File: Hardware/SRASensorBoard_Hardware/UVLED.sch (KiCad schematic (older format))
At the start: 8 parts

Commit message: Sciency stuff for the board
finished!
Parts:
- added D?: LED, Diode_SMD:D_0603_1608Metric_Pad1.05x0.95mm_HandSolder, symbol Device:LED
- added R?: 330, Resistor_SMD:R_0603_1608Metric_Pad1.05x0.95mm_HandSolder, symbol Device:R
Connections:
- net GND: now also D?.1 (K)
- net LED_Enable: now also R?.1
- new net: D?.2 (A), R?.2
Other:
- note added: "YELLOW"
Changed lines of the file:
@@
 Wire Wire Line
 	6350 3350 6500 3350
-Text GLabel 5250 3850 0    50   Input ~ 0
+Text GLabel 5125 4025 2    50   Input ~ 0
 LED_Enable
 $Comp
@@
 $EndComp
 Wire Wire Line
-	5250 3850 5350 3850
-Wire Wire Line
 	5750 3500 5750 3850
 Wire Wire Line
@@
 Wire Wire Line
 	4900 3050 6100 3050
+$Comp
+L Device:LED D?
+U 1 1 604F1096
+P 4550 3850
+AR Path="/604F1096" Ref="D?"  Part="1"
+AR Path="/5F841BF9/604F1096" Ref="D?"  Part="1"
+F 0 "D?" V 4589 3733 50  0000 R CNN
+F 1 "LED" V 4498 3733 50  0000 R CNN
+F 2 "Diode_SMD:D_0603_1608Metric_Pad1.05x0.95mm_HandSolder" H 4550 3850 50  0001 C CNN
+F 3 "~" H 4550 3850 50  0001 C CNN
+	1    4550 3850
+	1    0    0    -1
+$EndComp
+$Comp
+L Device:R R?
+U 1 1 604F109C
+P 4950 3850
+AR Path="/604F109C" Ref="R?"  Part="1"
+AR Path="/5F841BF9/604F109C" Ref="R?"  Part="1"
+F 0 "R?" H 5020 3896 50  0000 L CNN
+F 1 "330" H 5020 3805 50  0000 L CNN
+F 2 "Resistor_SMD:R_0603_1608Metric_Pad1.05x0.95mm_HandSolder" V 4880 3850 50  0001 C CNN
+F 3 "~" H 4950 3850 50  0001 C CNN
+	1    4950 3850
+	0    1    1    0
+$EndComp
+Text Notes 3875 3950 0    50   ~ 0
+YELLOW
+Wire Wire Line
+	4700 3850 4800 3850
+$Comp
+L power:GND #PWR?
+U 1 1 604F1131
+P 4250 3950
+AR Path="/604F1131" Ref="#PWR?"  Part="1"
+AR Path="/5F841BF9/604F1131" Ref="#PWR?"  Part="1"
+F 0 "#PWR?" H 4250 3700 50  0001 C CNN
+F 1 "GND" H 4350 3850 50  0000 C CNN
+F 2 "" H 4250 3950 50  0001 C CNN
+F 3 "" H 4250 3950 50  0001 C CNN
+	1    4250 3950
+	1    0    0    -1
+$EndComp
+Wire Wire Line
+	5100 3850 5125 3850
+Wire Wire Line
+	4250 3850 4250 3950
+Wire Wire Line
+	4250 3850 4400 3850
+Wire Wire Line
+	5125 4025 5125 3850
+Connection ~ 5125 3850
+Wire Wire Line
+	5125 3850 5350 3850
 $EndSCHEMATC

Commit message: Science_sensor reveiw 1
Yep
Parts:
- Q8: renamed from Q?; footprint Package_TO_SOT_SMD:SOT-23 -> Package_TO_SOT_SMD:TO-252-2
- gave numbers to parts that had none: 8
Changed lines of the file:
@@
 P 6250 3050
 AR Path="/5F8D9123" Ref="R?"  Part="1"
-AR Path="/5F8CBD9C/5F8D9123" Ref="R?"  Part="1"
+AR Path="/5F8CBD9C/5F8D9123" Ref="R37"  Part="1"
 AR Path="/5F8FEC08/5F8D9123" Ref="R?"  Part="1"
-F 0 "R?" V 6150 3050 50  0000 C CNN
+F 0 "R37" V 6150 3050 50  0000 C CNN
 F 1 "4" V 6250 3050 50  0000 C CNN
 F 2 "Resistor_THT:R_Axial_DIN0414_L11.9mm_D4.5mm_P15.24mm_Horizontal" V 6180 3050 50  0001 C CNN
@@
 P 6350 3350
 AR Path="/5F8D912A" Ref="#PWR?"  Part="1"
-AR Path="/5F8CBD9C/5F8D912A" Ref="#PWR?"  Part="1"
+AR Path="/5F8CBD9C/5F8D912A" Ref="#PWR0162"  Part="1"
 AR Path="/5F8FEC08/5F8D912A" Ref="#PWR?"  Part="1"
-F 0 "#PWR?" H 6350 3100 50  0001 C CNN
+F 0 "#PWR0162" H 6350 3100 50  0001 C CNN
 F 1 "GND" H 6355 3177 50  0000 C CNN
 F 2 "" H 6350 3350 50  0001 C CNN
@@
 P 6900 2950
 AR Path="/5F8D9132" Ref="Conn?"  Part="2"
-AR Path="/5F8CBD9C/5F8D9132" Ref="Conn?"  Part="2"
+AR Path="/5F8CBD9C/5F8D9132" Ref="Conn9"  Part="2"
 AR Path="/5F8FEC08/5F8D9132" Ref="Conn?"  Part="2"
-F 0 "Conn?" H 6872 2997 60  0000 R CNN
+F 0 "Conn9" H 6872 2997 60  0000 R CNN
 F 1 "UV_led" H 6872 3103 60  0000 R CNN
 F 2 "MRDT_Connectors:Anderson_2_Horizontal_Side_by_Side" H 6750 2400 60  0001 C CNN
@@
 P 6900 3250
 AR Path="/5F8D9138" Ref="Conn?"  Part="1"
-AR Path="/5F8CBD9C/5F8D9138" Ref="Conn?"  Part="1"
+AR Path="/5F8CBD9C/5F8D9138" Ref="Conn9"  Part="1"
 AR Path="/5F8FEC08/5F8D9138" Ref="Conn?"  Part="1"
-F 0 "Conn?" H 6872 3297 60  0000 R CNN
+F 0 "Conn9" H 6872 3297 60  0000 R CNN
 F 1 "UV_led" H 6872 3403 60  0000 R CNN
 F 2 "MRDT_Connectors:Anderson_2_Horizontal_Side_by_Side" H 6750 2700 60  0001 C CNN
@@
 P 4700 3150
 AR Path="/5F8D913E" Ref="Q?"  Part="1"
-AR Path="/5F8CBD9C/5F8D913E" Ref="Q?"  Part="1"
+AR Path="/5F8CBD9C/5F8D913E" Ref="Q7"  Part="1"
 AR Path="/5F8FEC08/5F8D913E" Ref="Q?"  Part="1"
-F 0 "Q?" V 5043 3150 50  0000 C CNN
+F 0 "Q7" V 5043 3150 50  0000 C CNN
 F 1 "Q_PMOS_GDS" V 4952 3150 50  0000 C CNN
 F 2 "Package_TO_SOT_SMD:TO-252-2" H 4900 3250 50  0001 C CNN
@@
 P 5350 3600
 AR Path="/5F8D9144" Ref="Q?"  Part="1"
-AR Path="/5F8CBD9C/5F8D9144" Ref="Q?"  Part="1"
+AR Path="/5F8CBD9C/5F8D9144" Ref="Q8"  Part="1"
 AR Path="/5F8FEC08/5F8D9144" Ref="Q?"  Part="1"
-F 0 "Q?" V 5700 3550 50  0000 L CNN
+F 0 "Q8" V 5700 3550 50  0000 L CNN
 F 1 "Q_NMOS_GSD" V 5600 3350 50  0000 L CNN
-F 2 "Package_TO_SOT_SMD:SOT-23" H 5550 3700 50  0001 C CNN
+F 2 "Package_TO_SOT_SMD:TO-252-2" H 5550 3700 50  0001 C CNN
 F 3 "~" H 5350 3600 50  0001 C CNN
 	1    5350 3600
@@
 P 4500 3500
 AR Path="/5F8D914A" Ref="R?"  Part="1"
-AR Path="/5F8CBD9C/5F8D914A" Ref="R?"  Part="1"
+AR Path="/5F8CBD9C/5F8D914A" Ref="R33"  Part="1"
 AR Path="/5F8FEC08/5F8D914A" Ref="R?"  Part="1"
-F 0 "R?" V 4600 3450 50  0000 L CNN
+F 0 "R33" V 4600 3450 50  0000 L CNN
 F 1 "22k" V 4500 3500 50  0000 C CNN
 F 2 "Resistor_SMD:R_0603_1608Metric_Pad1.05x0.95mm_HandSolder" V 4430 3500 50  0001 C CNN
@@
 P 4900 3500
 AR Path="/5F8D9150" Ref="R?"  Part="1"
-AR Path="/5F8CBD9C/5F8D9150" Ref="R?"  Part="1"
+AR Path="/5F8CBD9C/5F8D9150" Ref="R34"  Part="1"
 AR Path="/5F8FEC08/5F8D9150" Ref="R?"  Part="1"
-F 0 "R?" V 5000 3450 50  0000 L CNN
+F 0 "R34" V 5000 3450 50  0000 L CNN
 F 1 "22k" V 4900 3500 50  0000 C CNN
 F 2 "Resistor_SMD:R_0603_1608Metric_Pad1.05x0.95mm_HandSolder" V 4830 3500 50  0001 C CNN
@@
 P 5750 3950
 AR Path="/5F8D915B" Ref="#PWR?"  Part="1"
-AR Path="/5F8CBD9C/5F8D915B" Ref="#PWR?"  Part="1"
+AR Path="/5F8CBD9C/5F8D915B" Ref="#PWR0163"  Part="1"
 AR Path="/5F8FEC08/5F8D915B" Ref="#PWR?"  Part="1"
-F 0 "#PWR?" H 5750 3700 50  0001 C CNN
+F 0 "#PWR0163" H 5750 3700 50  0001 C CNN
 F 1 "GND" H 5755 3777 50  0000 C CNN
 F 2 "" H 5750 3950 50  0001 C CNN
@@
 P 5550 3850
 AR Path="/5F8D9162" Ref="R?"  Part="1"
-AR Path="/5F8CBD9C/5F8D9162" Ref="R?"  Part="1"
+AR Path="/5F8CBD9C/5F8D9162" Ref="R36"  Part="1"
 AR Path="/5F8FEC08/5F8D9162" Ref="R?"  Part="1"
-F 0 "R?" V 5450 3800 50  0000 L CNN
+F 0 "R36" V 5450 3800 50  0000 L CNN
 F 1 "10k" V 5550 3850 50  0000 C CNN
 F 2 "Resistor_SMD:R_0603_1608Metric_Pad1.05x0.95mm_HandSolder" V 5480 3850 50  0001 C CNN
@@
 P 4200 3000
 AR Path="/5F8D9170" Ref="#PWR?"  Part="1"
-AR Path="/5F8CBD9C/5F8D9170" Ref="#PWR?"  Part="1"
+AR Path="/5F8CBD9C/5F8D9170" Ref="#PWR0164"  Part="1"
 AR Path="/5F8FEC08/5F8D9170" Ref="#PWR?"  Part="1"
-F 0 "#PWR?" H 4200 2850 50  0001 C CNN
+F 0 "#PWR0164" H 4200 2850 50  0001 C CNN
 F 1 "+24V" H 4215 3173 50  0000 C CNN
 F 2 "" H 4200 3000 50  0001 C CNN
@@
 AR Path="/604F1096" Ref="D?"  Part="1"
 AR Path="/5F841BF9/604F1096" Ref="D?"  Part="1"
-F 0 "D?" V 4589 3733 50  0000 R CNN
+AR Path="/5F8CBD9C/604F1096" Ref="D19"  Part="1"
+F 0 "D19" V 4589 3733 50  0000 R CNN
 F 1 "LED" V 4498 3733 50  0000 R CNN
 F 2 "Diode_SMD:D_0603_1608Metric_Pad1.05x0.95mm_HandSolder" H 4550 3850 50  0001 C CNN
@@
 AR Path="/604F109C" Ref="R?"  Part="1"
 AR Path="/5F841BF9/604F109C" Ref="R?"  Part="1"
-F 0 "R?" H 5020 3896 50  0000 L CNN
+AR Path="/5F8CBD9C/604F109C" Ref="R35"  Part="1"
+F 0 "R35" H 5020 3896 50  0000 L CNN
 F 1 "330" H 5020 3805 50  0000 L CNN
 F 2 "Resistor_SMD:R_0603_1608Metric_Pad1.05x0.95mm_HandSolder" V 4880 3850 50  0001 C CNN
@@
 AR Path="/604F1131" Ref="#PWR?"  Part="1"
 AR Path="/5F841BF9/604F1131" Ref="#PWR?"  Part="1"
-F 0 "#PWR?" H 4250 3700 50  0001 C CNN
+AR Path="/5F8CBD9C/604F1131" Ref="#PWR0165"  Part="1"
+F 0 "#PWR0165" H 4250 3700 50  0001 C CNN
 F 1 "GND" H 4350 3850 50  0000 C CNN
 F 2 "" H 4250 3950 50  0001 C CNN

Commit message: Fixed some library issues
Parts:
- R33, R34, R36: footprint Resistor_SMD:R_0603_1608Metric_Pad1.05x0.95mm_HandSolder -> Resistor_SMD:R_0603_1608Metric_Pad0.98x0.95mm_HandSolder
- R35: value 330 -> 480; footprint Resistor_SMD:R_0603_1608Metric_Pad1.05x0.95mm_HandSolder -> Resistor_SMD:R_0603_1608Metric_Pad0.98x0.95mm_HandSolder
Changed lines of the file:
@@
 EESchema Schematic File Version 4
+LIBS:SRA_Sensor_Board-cache
 EELAYER 30 0
 EELAYER END
@@
 F 0 "R33" V 4600 3450 50  0000 L CNN
 F 1 "22k" V 4500 3500 50  0000 C CNN
-F 2 "Resistor_SMD:R_0603_1608Metric_Pad1.05x0.95mm_HandSolder" V 4430 3500 50  0001 C CNN
+F 2 "Resistor_SMD:R_0603_1608Metric_Pad0.98x0.95mm_HandSolder" V 4430 3500 50  0001 C CNN
 F 3 "~" H 4500 3500 50  0001 C CNN
 	1    4500 3500
@@
 F 0 "R34" V 5000 3450 50  0000 L CNN
 F 1 "22k" V 4900 3500 50  0000 C CNN
-F 2 "Resistor_SMD:R_0603_1608Metric_Pad1.05x0.95mm_HandSolder" V 4830 3500 50  0001 C CNN
+F 2 "Resistor_SMD:R_0603_1608Metric_Pad0.98x0.95mm_HandSolder" V 4830 3500 50  0001 C CNN
 F 3 "~" H 4900 3500 50  0001 C CNN
 	1    4900 3500
@@
 F 0 "R36" V 5450 3800 50  0000 L CNN
 F 1 "10k" V 5550 3850 50  0000 C CNN
-F 2 "Resistor_SMD:R_0603_1608Metric_Pad1.05x0.95mm_HandSolder" V 5480 3850 50  0001 C CNN
+F 2 "Resistor_SMD:R_0603_1608Metric_Pad0.98x0.95mm_HandSolder" V 5480 3850 50  0001 C CNN
 F 3 "~" H 5550 3850 50  0001 C CNN
 	1    5550 3850
@@
 AR Path="/5F8CBD9C/604F109C" Ref="R35"  Part="1"
 F 0 "R35" H 5020 3896 50  0000 L CNN
-F 1 "330" H 5020 3805 50  0000 L CNN
-F 2 "Resistor_SMD:R_0603_1608Metric_Pad1.05x0.95mm_HandSolder" V 4880 3850 50  0001 C CNN
+F 1 "480" H 5020 3805 50  0000 L CNN
+F 2 "Resistor_SMD:R_0603_1608Metric_Pad0.98x0.95mm_HandSolder" V 4880 3850 50  0001 C CNN
 F 3 "~" H 4950 3850 50  0001 C CNN
 	1    4950 3850

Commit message: Finished BOM
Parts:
- D19: value LED -> Yellow
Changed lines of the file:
@@
 AR Path="/5F8CBD9C/604F1096" Ref="D19"  Part="1"
 F 0 "D19" V 4589 3733 50  0000 R CNN
-F 1 "LED" V 4498 3733 50  0000 R CNN
+F 1 "Yellow" V 4498 3733 50  0000 R CNN
 F 2 "Diode_SMD:D_0603_1608Metric_Pad1.05x0.95mm_HandSolder" H 4550 3850 50  0001 C CNN
 F 3 "~" H 4550 3850 50  0001 C CNN

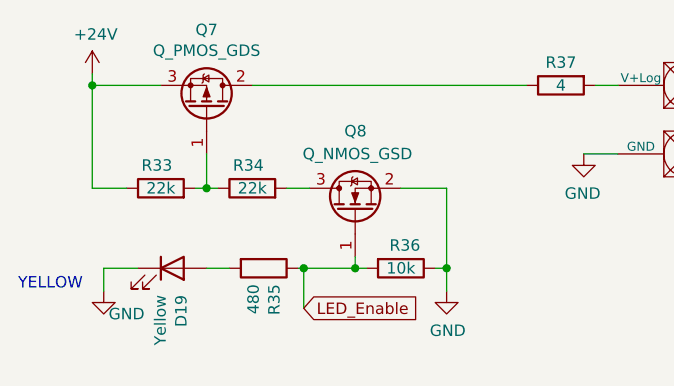
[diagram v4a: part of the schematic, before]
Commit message: Actually fixed the BOM
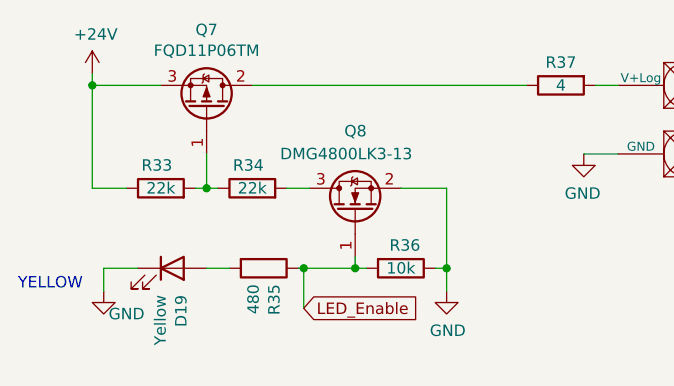
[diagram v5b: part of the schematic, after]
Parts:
- Q7: value Q_PMOS_GDS -> ‎FQD11P06TM‎
- Q8: value Q_NMOS_GSD -> DMG4800LK3-13‎
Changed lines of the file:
@@
 AR Path="/5F8FEC08/5F8D913E" Ref="Q?"  Part="1"
 F 0 "Q7" V 5043 3150 50  0000 C CNN
-F 1 "Q_PMOS_GDS" V 4952 3150 50  0000 C CNN
+F 1 "‎FQD11P06TM‎" V 4952 3150 50  0000 C CNN
 F 2 "Package_TO_SOT_SMD:TO-252-2" H 4900 3250 50  0001 C CNN
 F 3 "~" H 4700 3150 50  0001 C CNN
@@
 AR Path="/5F8FEC08/5F8D9144" Ref="Q?"  Part="1"
 F 0 "Q8" V 5700 3550 50  0000 L CNN
-F 1 "Q_NMOS_GSD" V 5600 3350 50  0000 L CNN
+F 1 "DMG4800LK3-13‎ " V 5600 3350 50  0000 L CNN
 F 2 "Package_TO_SOT_SMD:TO-252-2" H 5550 3700 50  0001 C CNN
 F 3 "~" H 5350 3600 50  0001 C CNN
